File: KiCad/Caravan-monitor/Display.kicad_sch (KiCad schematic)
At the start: 7 parts, among them Q1 2N7002, U1 NHD-C0220BIZ

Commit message: Schematics done
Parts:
- C22, C23, C24: footprint Capacitor_SMD:C_0805_2012Metric_Pad1.18x1.45mm_HandSolder -> Capacitor_SMD:C_0402_1005Metric_Pad0.74x0.62mm_HandSolder
- R21, R22: footprint Resistor_SMD:R_0805_2012Metric_Pad1.20x1.40mm_HandSolder -> Resistor_SMD:R_0402_1005Metric_Pad0.72x0.64mm_HandSolder

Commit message: PCB Designed
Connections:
- net BL_Anode: now reaches R21.2, U1.9 (A)
- net BL_Cathode: now reaches Q1.3 (D), U1.10 (K)
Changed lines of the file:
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@@
+		)
+	)
+	(label "BL_Cathode"
+		(at 143.51 99.06 270)
+		(effects
+			(font
+				(size 1.27 1.27)
+			)
+			(justify right bottom)
+		)
+	)
+	(label "BL_Anode"
+		(at 140.97 95.25 0)
+		(effects
+			(font
+				(size 1.27 1.27)
+			)
+			(justify left bottom)
 		)
 	)

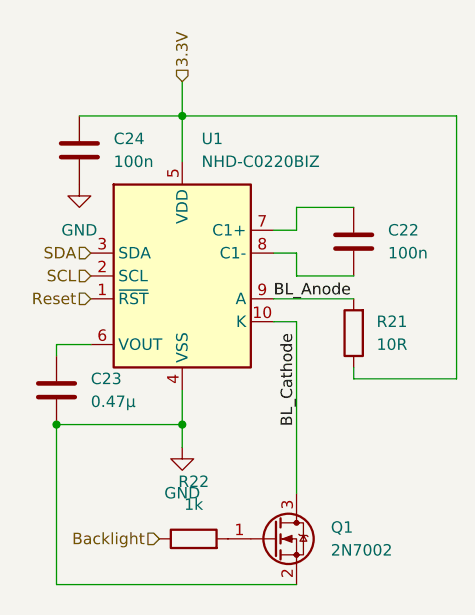
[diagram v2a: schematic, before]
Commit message: Schematic updates
Parts changed for JLCPCB assembly compatibility
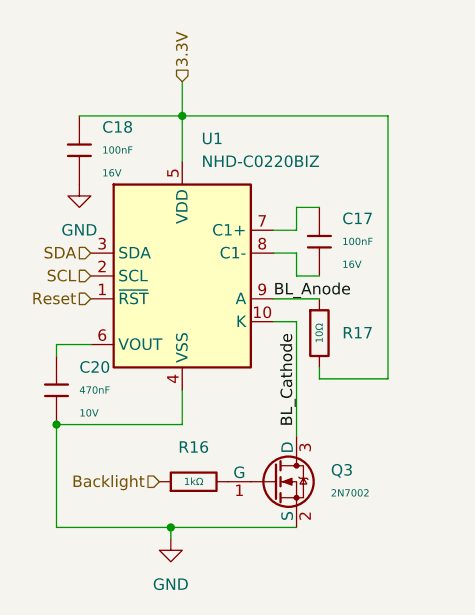
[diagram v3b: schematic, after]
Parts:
- removed C22, C24: 100n, Capacitor_SMD:C_0402_1005Metric_Pad0.74x0.62mm_HandSolder, symbol Device:C
- removed C23: 0.47µ, Capacitor_SMD:C_0402_1005Metric_Pad0.74x0.62mm_HandSolder, symbol Device:C
- removed Q1: 2N7002, Package_TO_SOT_SMD:SOT-23_Handsoldering, symbol Transistor_FET:2N7002
- removed R21: 10R, Resistor_SMD:R_0402_1005Metric_Pad0.72x0.64mm_HandSolder, symbol Device:R
- removed R22: 1k, Resistor_SMD:R_0402_1005Metric_Pad0.72x0.64mm_HandSolder, symbol Device:R
- added C17, C18: 100nF, PCM_JLCPCB:C_0402, symbol PCM_JLCPCB-Capacitors:0402,100nF
- added C20: 470nF, PCM_JLCPCB:C_0402, symbol PCM_JLCPCB-Capacitors:0402,470nF
- added Q3: 2N7002, PCM_JLCPCB:Q_SOT-23, symbol PCM_JLCPCB-Transistors:NMOS,2N7002
- added R16: 1kΩ, PCM_JLCPCB:R_0402, symbol PCM_JLCPCB-Resistors:0402,1kΩ
- added R17: 10Ω, PCM_JLCPCB:R_0603, symbol PCM_JLCPCB-Resistors:0603,10Ω
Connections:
- net 3.3V: now also C18.1, R17.2
- net BL_Anode: now also R17.1
- net BL_Cathode: now also Q3.3 (D)
- net Backlight: now also R16.1
- net GND: now also C18.2, C20.2, Q3.2 (S)
- net at U1.7 (C1+): now also C17.1
- net at U1.8 (C1-): now also C17.2
- net at U1.6 (VOUT): now also C20.1
- new net: Q3.1 (G), R16.2
